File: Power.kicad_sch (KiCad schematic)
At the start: 99 parts, among them Q3 FDMC510P, U1 ZXCT1009F, U2 LT1763, U3 TPS62110, U33 TPS82150, U34 LT3097, U35 LT8582

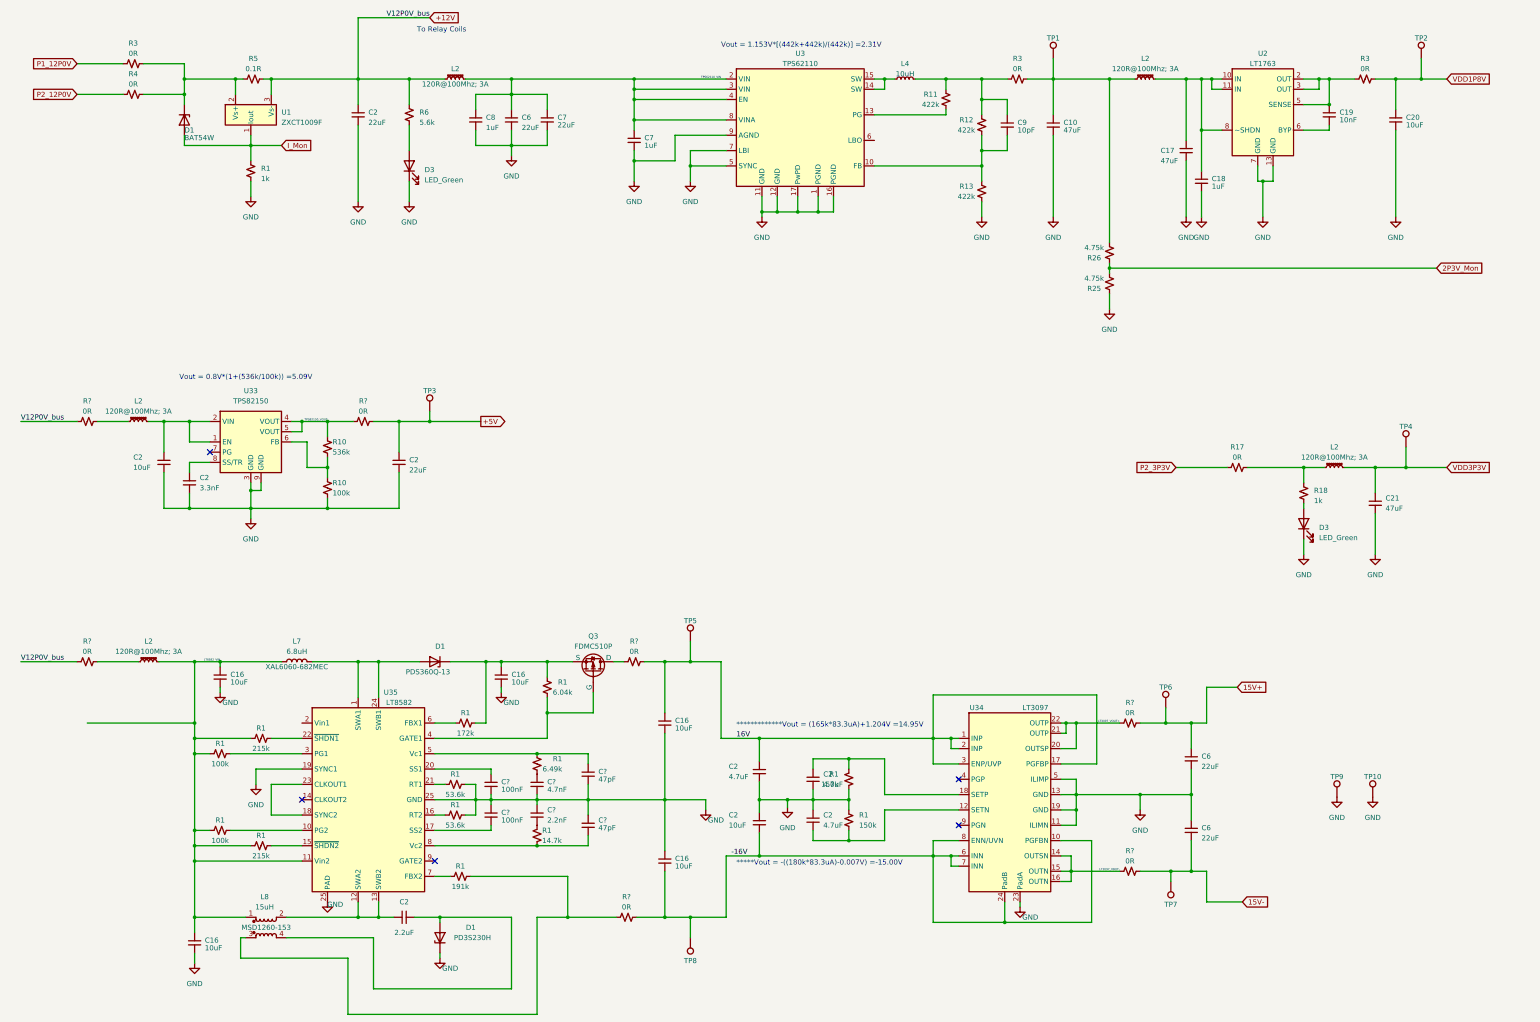
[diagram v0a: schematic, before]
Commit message: Updated Schematics with all suggestions
-Added pull up resistors on SDO line to FPGA
-Fixed some I/O flags to properly indicate direction
-Added Bulk caps on 15V rails
-Added series caps to AC couple the LVDS clock lines. See AN408 from the manufacture
-Add Voltage monitor for 1.8V and 5V
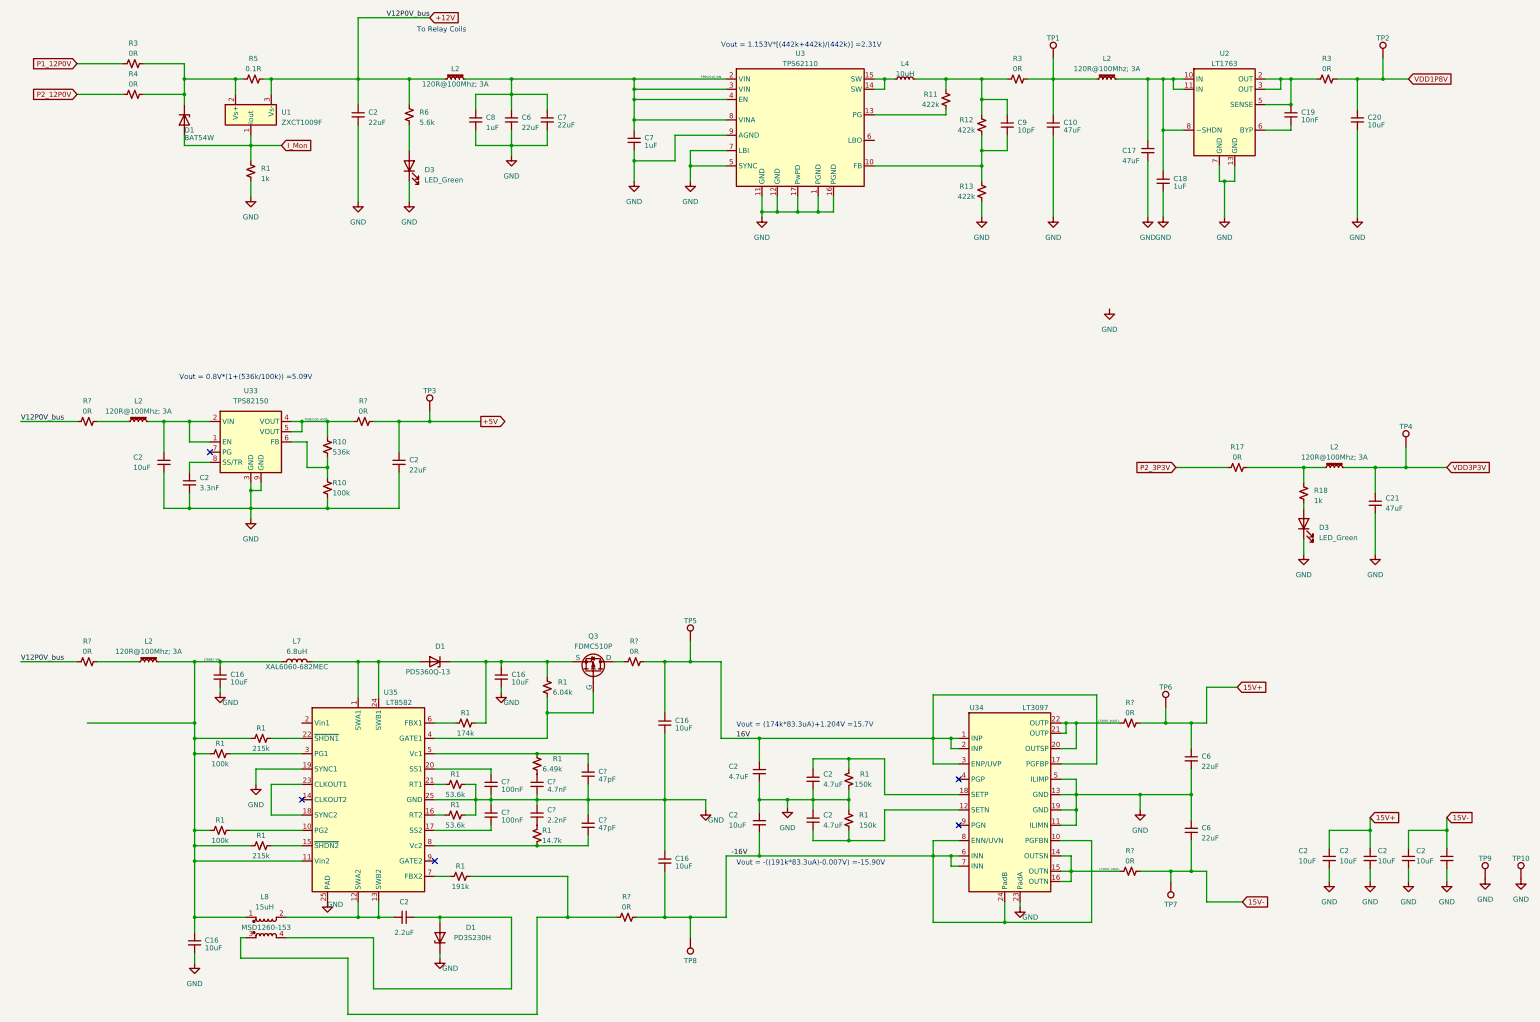
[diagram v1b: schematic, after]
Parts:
- removed R25, R26: 4.75k, Resistor_SMD:R_0603_1608Metric, symbol Device:R_Small_US
- added C2 (x4): 10uF, Capacitor_SMD:C_0805_2012Metric, symbol Device:C_Small
- R1: value 172k -> 174k
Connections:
- net 15V+: now also C2.1, C2.1
- net 15V-: now also C2.1, C2.1
- net GND: now also C2.2, C2.2, C2.2, C2.2
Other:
- note added: "Vout = (174k*83.3uA)+1.204V =15.7V"
- note added: "Vout = -((191k*83.3uA)-0.007V) =-15.90V"
- note removed: "*************Vout = (165k*83.3uA)+1.204V =14.95V"
- note removed: "*****Vout = -((180k*83.3uA)-0.007V) =-15.00V"
- moved on the sheet: C17, C18, C19, C20, L2, R3, TP10, TP2, TP9, U2

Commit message: Updated Project
Schematics:
-updated level shifting IC's
-Add notes to level shifters
-Changed Relay Coil Driver channel mapping
-Added additional Mounting Hole

Layout
-WIP To Complete:
-Relay Driver ICs
- Reworking LT8582 area
- Level Shifters
- Housekeeping ICs
-Misc. error cleanup
- Silkscreen adjust
- Add Silkscreen SN & logo
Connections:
- net LT8582_VIN: now also U35.2 (Vin1)
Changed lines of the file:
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@@
     (stroke (width 0) (type default))
   )
-  (wire (pts (xy 64.77 195.58) (xy 38.1 195.58))
+  (wire (pts (xy 64.77 195.58) (xy 91.44 195.58))
     (stroke (width 0) (type default))
   )
@@
       )
       (project "Quartz_v1p1"
-        (path "/674e1e7f-67ba-4e85-a926-dcd5f6a22021/db3c7ba2-982f-432b-8742-662861d58c3e"
-          (reference "D2") (unit 1)
-        )
         (path "/674e1e7f-67ba-4e85-a926-dcd5f6a22021/ac1e64b2-1a26-4ac8-9188-8b2d840a4cd2"
           (reference "D6") (unit 1)
@@
       )
       (project "Quartz_v1p1"
-        (path "/674e1e7f-67ba-4e85-a926-dcd5f6a22021/db3c7ba2-982f-432b-8742-662861d58c3e"
-          (reference "D2") (unit 1)
-        )
         (path "/674e1e7f-67ba-4e85-a926-dcd5f6a22021/ac1e64b2-1a26-4ac8-9188-8b2d840a4cd2"
           (reference "D5") (unit 1)

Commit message: Updated Project with Latest Changes
Project:
-Added pdf plots of PCB layout

Schematics:
-Fixed L8 Pinout
-Adjusted FMC connections
-Adjusted level shifter connections

Layout:
-Completed AFE/ADC/Power/Relay driver sections

Layout WIP To Complete:
-Misc. error cleanup
- Silkscreen adjust
- Add Silkscreen SN & logo
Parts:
- removed C2 (x4): 10uF, Capacitor_SMD:C_0805_2012Metric, symbol Device:C_Small
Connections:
- net at C2.1, U35.12 (SWA2), U35.13 (SWB2): now also L8.3; no longer L8.2
- net at R1.2, R?.1: now also L8.2; no longer L8.3

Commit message: Push Version before ADC change from 1.8V to 2.5V I/O
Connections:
- net I_Mon renamed I_MON
- no-connect marks 5 -> 6
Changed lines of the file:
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@@
   (no_connect (at 254.635 220.98))
   (no_connect (at 91.44 214.63))
+  (no_connect (at 233.68 50.8))
   (no_connect (at 68.58 128.27))
   (wire (pts (xy 73.66 203.2) (xy 91.44 203.2))
@@
     )
   )
-  (global_label "I_Mon" (shape input) (at 86.36 52.07 0) (fields_autoplaced)
+  (global_label "I_MON" (shape input) (at 86.36 52.07 0) (fields_autoplaced)
     (effects (font (size 1.27 1.27)) (justify left))
-    (property "Intersheetrefs" "${INTERSHEET_REFS}" (at 94.5876 52.07 0)
+    (property "Intersheetrefs" "${INTERSHEET_REFS}" (at 94.9506 52.07 0)
       (effects (font (size 1.27 1.27)) (justify left) hide)
     )
@@
   (global_label "+12V" (shape input) (at 123.19 20.32 0) (fields_autoplaced)
     (effects (font (size 1.27 1.27)) (justify left))
-    (property "Intersheetrefs" "${INTERSHEET_REFS}" (at 131.2552 20.32 0)
+    (property "Intersheetrefs" "${INTERSHEET_REFS}" (at 131.1758 20.32 0)
       (effects (font (size 1.27 1.27)) (justify left) hide)
     )
@@
         )
       )
-    )
-  )
-  (symbol (lib_id "power:GND") (at 292.1 92.71 0) (unit 1)
-    (in_bom yes) (on_board yes) (dnp no)
-    (property "Reference" "#PWR044" (at 292.1 99.06 0)
-      (effects (font (size 1.27 1.27)) hide)
-    )
-    (property "Value" "GND" (at 292.1 97.79 0)
-      (effects (font (size 1.27 1.27)))
-    )
-    (property "Footprint" "" (at 292.1 92.71 0)
-      (effects (font (size 1.27 1.27)) hide)
-    )
-    (property "Datasheet" "" (at 292.1 92.71 0)
-      (effects (font (size 1.27 1.27)) hide)
-    )
-    (pin "1")
-    (instances
-      (project "Zest_MPEX_v1p3"
-        (path "/00cb7cb7-8be2-4970-8959-a06932b2fa76/bd960755-3e45-476f-84b6-fdf0c21cce40"
-          (reference "#PWR044") (unit 1)
-        )
-      )
-      (project "Quartz_v1p1"
-        (path "/674e1e7f-67ba-4e85-a926-dcd5f6a22021/ac1e64b2-1a26-4ac8-9188-8b2d840a4cd2"
-          (reference "#PWR0192") (unit 1)
-        )
-      )

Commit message: Changed ADCs to run on +2.5V VADJ
Modified schematic to allow the ADCs to be run from the +2.5V VADJ inputs on the FMC connector.
-All relevant ERC issues ran been looked into.
-Still working on all Board DRC issues.
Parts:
- removed C10, C17: 47uF, Capacitor_SMD:C_0805_2012Metric, symbol Device:C_Small
- removed C18, C7, C8: 1uF, Capacitor_SMD:C_0603_1608Metric, symbol Device:C_Small
- removed C19: 10nF, Capacitor_SMD:C_0603_1608Metric, symbol Device:C_Small
- removed C20: 10uF, Capacitor_SMD:C_0805_2012Metric, symbol Device:C_Small
- removed C6, C7: 22uF, Capacitor_SMD:C_0805_2012Metric, symbol Device:C_Small
- removed C9: 10pF, Capacitor_SMD:C_0603_1608Metric, symbol Device:C_Small
- removed L2 (x2): 120R@100Mhz; 3A, Inductor_SMD:L_0805_2012Metric, symbol Device:L_Ferrite_Small
- removed L4: 10uH, footprints:IND_7345-WE-PD_WRE, symbol Device:L_Small
- removed R11, R12, R13: 422k, Resistor_SMD:R_0603_1608Metric, symbol Device:R_Small_US
- removed R3 (x2): 0R, Resistor_SMD:R_0603_1608Metric, symbol Device:R_Small_US
- removed TP1, TP2: ~, TestPoint:TestPoint_Loop_D1.80mm_Drill1.0mm_Beaded, symbol Connector:TestPoint
- removed U2: LT1763, Package_DFN_QFN:DFN-12-1EP_3x4mm_P0.5mm_EP1.7x3.3mm, symbol Custom_Lib_MPEX_Zest:LT1763_12pin
- removed U3: TPS62110, Package_DFN_QFN:QFN-16-1EP_4x4mm_P0.65mm_EP2.7x2.7mm_PullBack, symbol Custom_Lib_MPEX_Zest:TPS62110
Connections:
- no-connect marks 6 -> 5
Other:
- note removed: "Vout = 1.153V*[(442k+442k)/(442k)] =2.31V"

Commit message: Completed Schmatic and Layout
All Schematic and Layout Task are complete with the following exceptions:
- Adjust Silkscreen Layers
- Add Osprey Logo and Serial Number

Note-Removed Files no longer reference in the project
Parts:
- added C21 (x2): 47uF, Capacitor_SMD:C_0805_2012Metric, symbol Device:C_Small
- added D3 (x2): LED_Green, LED_SMD:LED_0603_1608Metric, symbol Device:LED
- added L2 (x2): 120R@100Mhz; 3A, Inductor_SMD:L_0805_2012Metric, symbol Device:L_Ferrite_Small
- added R17 (x2): 0R, Resistor_SMD:R_0603_1608Metric, symbol Device:R_Small_US
- added R18 (x2): 1k, Resistor_SMD:R_0603_1608Metric, symbol Device:R_Small_US
- added TP1, TP2: ~, TestPoint:TestPoint_Loop_D1.80mm_Drill1.0mm_Beaded, symbol Connector:TestPoint
- D1: symbol Device:D_Zener -> AD7768_Digitizer_SLib:D_BAT54W
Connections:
- net GND: now also C21.2, C21.2, D3.1 (K), D3.1 (K)
- net I_MON: now also D1.1 (A); no longer D1.2 (A)
- net at R3.2, R4.2, R5.1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: now also D1.3 (K); no longer D1.1 (K)
- new net: L2.1, R17.2, R18.2 (x2)
- new net: D3.2 (A), R18.1 (x2)
- new net P1_2P5V: C21.1, L2.2, TP1.1
- new net P1_VADJ: R17.1
- new net P2_2P5V: C21.1, L2.2, TP2.1
- new net P2_VADJ: R17.1
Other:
- moved on the sheet: C16, C2, C21, C6, C?, D1, D3, L2, L7, L8, Q3, R1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

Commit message: Full upload of project as it was for prototype order
-Fixed issue with L7 footprint as pointed out by sierra circuits
-Updated all files with up to date info as it was ordered
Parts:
- C16, C2: MPN (none) -> GRM21BR61E106KA73L; Note X5R 25V 1206 -> (none)
- C2: MPN (none) -> TMK212AB7475KG-T; Note X5R 25V 1206 -> (none)
- C2: MPN (none) -> GRM1885C1H332JA01D; Note X5R 25V 1206 -> (none)
- C2: MPN GCJ31CR71H225KA12L -> GRM21BR71E225KE11L; Note X5R 50V 1206 -> (none)
- C2, C6: MPN (none) -> GRT21BR61E226ME13L; Note X5R 25V 1206 -> (none)
- C21: MPN (none) -> C2012X5R1A476M125AC; Note X5R 25V 1206 -> (none)
- C? (x2): MPN CL10B104KB8NNWC -> CL05A104KA5NNNC
- C? (x2): MPN (none) -> GRM1885C1H470JA01D
- C?: MPN CL10B104KB8NNWC -> CGA3E2C0G1H472J080AA
- C?: MPN CL10B104KB8NNWC -> GCM1885C1H222JA16D
- D1: footprint Diode_SMD:D_SOD-323_HandSoldering -> QuartzFootprints:D_SOD-323_HandSoldering; MPN (none) -> PD3S230H-7
- D1: footprint Diode_SMD:D_PowerDI-5 -> QuartzFootprints:D_PowerDI-5
- L2: value 120R@100Mhz; 3A -> 60R@100Mhz; 3.5A; MPN BLM18KG121TN1D -> BLM21PG600SN1D
- L7: footprint footprints:IND_7345-WE-PD_WRE -> QuartzFootprints:IND_7345-WE-PD_WRE
- L8: footprint footprints:MSD1260153MLD -> QuartzFootprints:MSD1260153MLD; MPN MSD1260-153 -> MSD1260-153MLD
- Q3: footprint footprints:MLP8_3P3X3P3_ONS-M -> QuartzFootprints:MLP8_3P3X3P3_ONS-M
- R1: MPN (none) -> RC0402FR-0753K6L
- R1: MPN (none) -> RC0603FR-076K49L
- R1: MPN (none) -> RC0603FR-07150KL
- R1: MPN (none) -> RC0402FR-07215KL
- R1: MPN (none) -> RC0603FR-07174KL
- R1: MPN (none) -> RC0805FR-071KL
- R1: MPN (none) -> RC0402FR-07100KL
- R1: MPN (none) -> RC0603FR-076K04L
- R1: MPN (none) -> RC0603FR-07191KL
- R1: MPN (none) -> RC0603FR-0714K7L
- R10: MPN (none) -> RC0603FR-07536KL
- R10: MPN (none) -> RC0603FR-07100KL
- R17, R? (x7): MPN (none) -> ERJ-3GEY0R00V
- R18: MPN (none) -> RC0603FR-071KL
- R3, R4: MPN (none) -> ERJ-6GEY0R00V
- R6: MPN (none) -> RC0603FR-075K6L
- TP1, TP2, TP3, TP4, TP5, TP6, TP7, TP8: MPN (none) -> 5000
- TP10, TP9: MPN (none) -> 5001
- U1: MPN ZXCT1009F -> ZXCT1009FTA
- U33: footprint footprints:SIL0008D_SMD -> QuartzFootprints:SIL0008D_SMD; MPN (none) -> TPS82150SILR
- U34: footprint footprints:05-08-7071_ADI-M -> QuartzFootprints:05-08-7071_ADI-M; MPN (none) -> LT3097ADJC#PBF
- U35: MPN LT8582 -> LT8582EDKD#TRPBF
